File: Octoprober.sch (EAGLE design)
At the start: 140 parts, among them J1 10118193-0001LF, J2 26-60-4020, P1 TC33X-2-103E, SW1 101-0134-EV, SW2 EVQ-Q2203W, SW3 EVQ-Q2203W, SW4 EVQ-Q2203W, SW5 EVQ-Q2203W, U1 P8X32A-M44, U10 MAX31855KASA+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

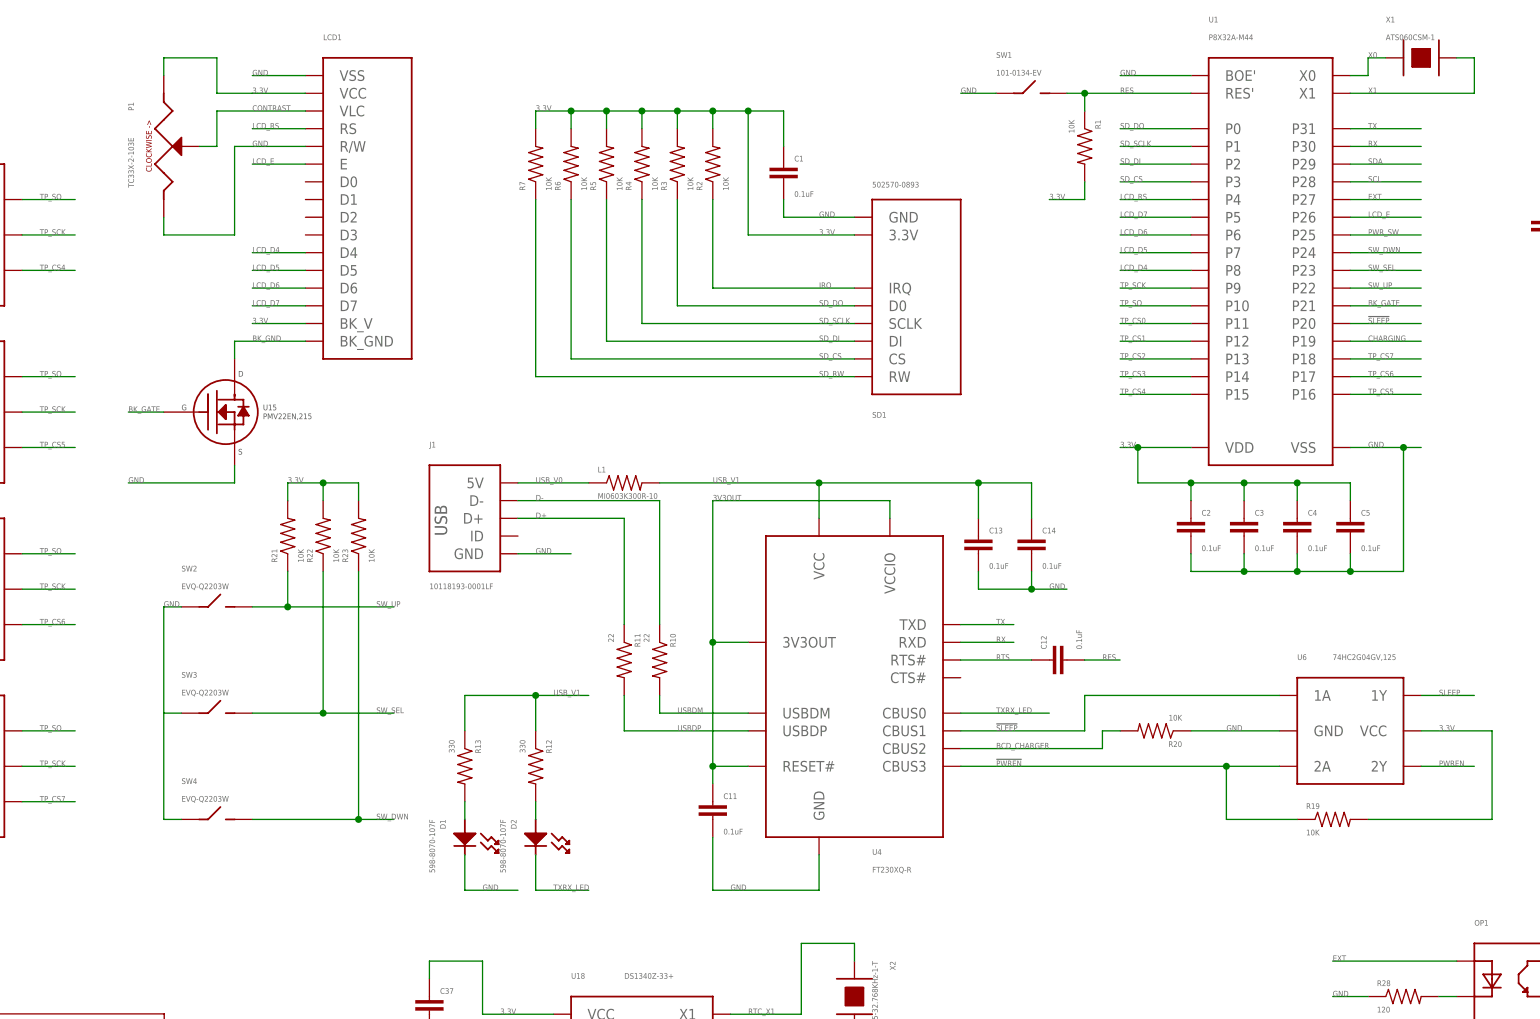
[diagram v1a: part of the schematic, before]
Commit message: Changed FT230X RST to be controlled by PROP
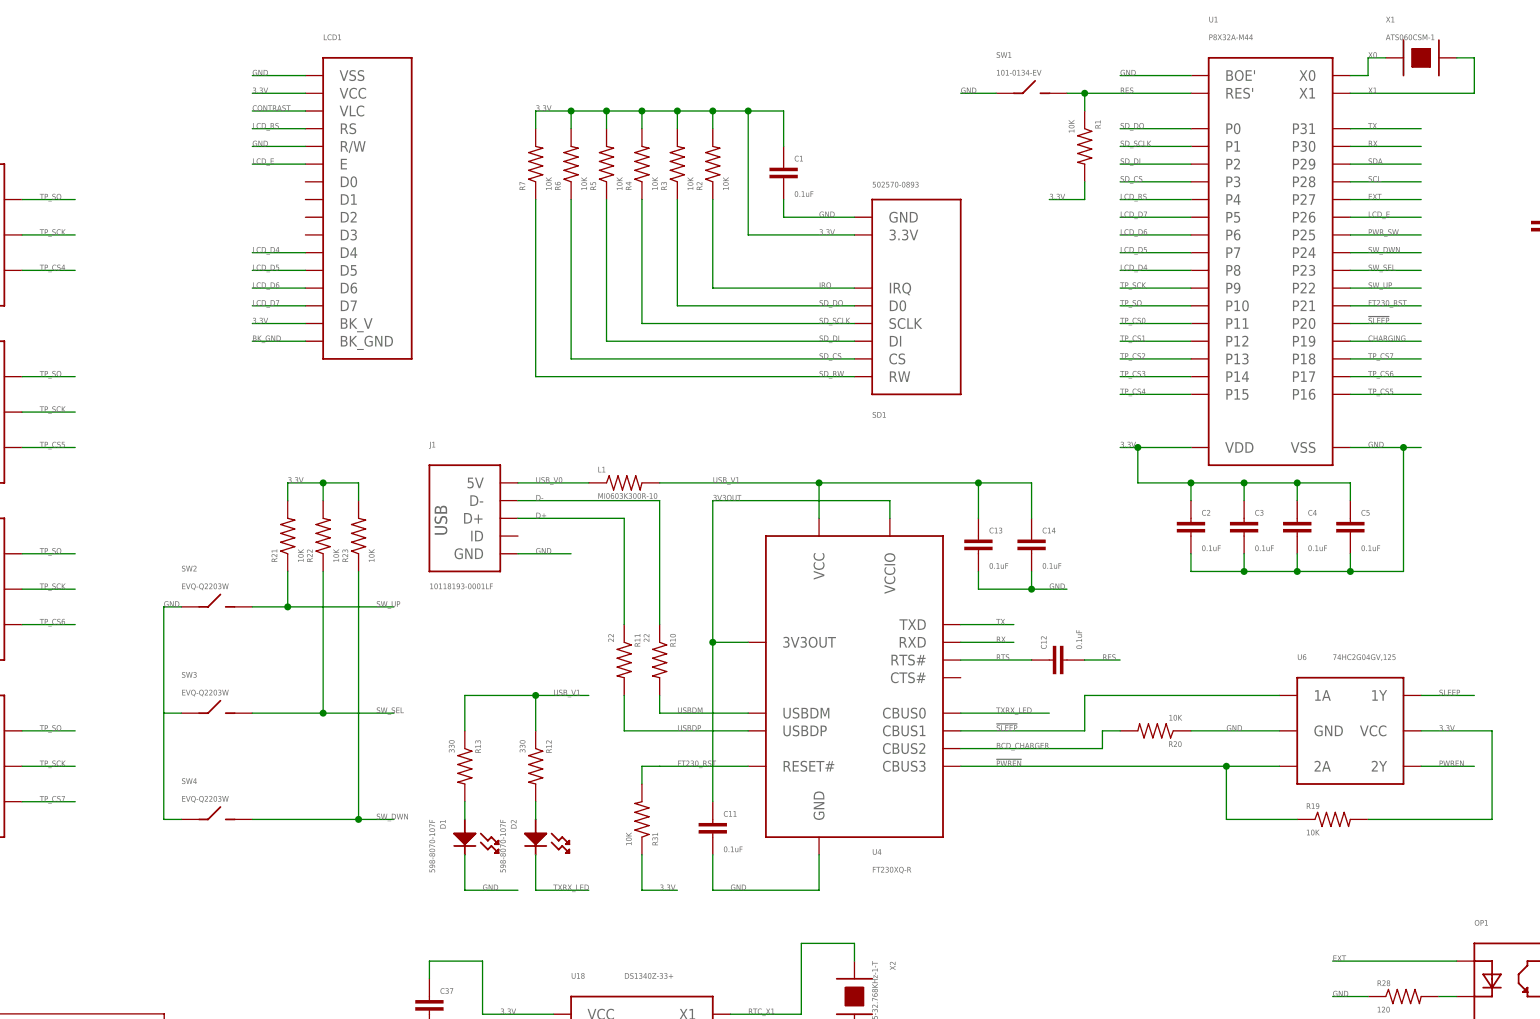
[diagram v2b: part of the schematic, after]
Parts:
- removed P1: TC33X-2-103E, PP_Passives:TC33X-1TC33X-1
- removed U15: PMV22EN,215, PP_DiscreteSemi:MOSFET_N-CHANNEL_SINGLESOT-23
- added R31: 10K, PP_Passives:RESISTOR0402
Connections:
- removed net BK_GATE: U1.P21, U15.GATE
- new net FT230_RST: R31.2, U1.P21, U4.RESET#
- net 3.3V: now also R31.1; no longer P1.1_CCW
- net 3V3OUT: no longer U4.RESET#
- net BK_GND: no longer U15.DRAIN
- net CONTRAST: no longer P1.2_WIPER
- net GND: no longer P1.3_CW, U15.SOURCE
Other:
- moved on the sheet: C11
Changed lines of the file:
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@@
 </part>
 <part name="LCD1" library="PP_Displays" deviceset="HD44780_LCD" device="1602_COUNTERSINK"/>
-<part name="P1" library="PP_Passives" deviceset="TC33X-1" device="TC33X-1" value="TC33X-2-103E"/>
 <part name="U7" library="PP_Sensors" deviceset="MAX31855" device="SO-8" value="MAX31855KASA+"/>
 <part name="C15" library="PP_Passives" deviceset="CAPACITOR_NON_POLAR" device="0402" value="0.1uF"/>
@@
 <part name="R19" library="PP_Passives" deviceset="RESISTOR" device="0402" value="10K"/>
 <part name="R20" library="PP_Passives" deviceset="RESISTOR" device="0402" value="10K"/>
-<part name="U15" library="PP_DiscreteSemi" deviceset="MOSFET_N-CHANNEL_SINGLE" device="SOT-23" value="PMV22EN,215"/>
 <part name="SW2" library="PP_Electromechanical" deviceset="SPST" device="EVQ-Q2203W" value="EVQ-Q2203W"/>
 <part name="SW3" library="PP_Electromechanical" deviceset="SPST" device="EVQ-Q2203W" value="EVQ-Q2203W"/>
@@
 <part name="C39" library="PP_Passives" deviceset="CAPACITOR_NON_POLAR" device="0402" value="0.1uF"/>
 <part name="U19" library="PP_DigitalIC" deviceset="MCP3021" device="SOT-23A" value="MCP3021A5T-E/OT"/>
+<part name="R31" library="PP_Passives" deviceset="RESISTOR" device="0402" value="10K"/>
 </parts>
 <sheets>
@@
 <instance part="L1" gate="G$1" x="-93.98" y="-27.94"/>
 <instance part="U4" gate="G$1" x="-60.96" y="-58.42"/>
-<instance part="C11" gate="G$1" x="-81.28" y="-73.66"/>
+<instance part="C11" gate="G$1" x="-81.28" y="-76.2"/>
 <instance part="R10" gate="G$1" x="-88.9" y="-53.34" rot="R270"/>
 <instance part="R11" gate="G$1" x="-93.98" y="-53.34" rot="R270"/>
@@
 </instance>
 <instance part="LCD1" gate="G$1" x="-129.54" y="12.7"/>
-<instance part="P1" gate="G$1" x="-160.02" y="20.32" rot="R270"/>
 <instance part="U7" gate="G$1" x="-292.1" y="7.62"/>
 <instance part="C15" gate="G$1" x="-325.12" y="10.16"/>
@@
 <instance part="R19" gate="G$1" x="7.62" y="-76.2"/>
 <instance part="R20" gate="G$1" x="-17.78" y="-63.5" rot="R180"/>
-<instance part="U15" gate="G$1" x="-149.86" y="-17.78"/>
 <instance part="SW2" gate="G$1" x="-152.4" y="-45.72"/>
 <instance part="SW3" gate="G$1" x="-152.4" y="-60.96"/>
@@
 <instance part="C39" gate="G$1" x="86.36" y="-116.84"/>
 <instance part="U19" gate="G$1" x="119.38" y="-109.22"/>
+<instance part="R31" gate="G$1" x="-91.44" y="-76.2" rot="MR90"/>
 </instances>
 <busses>
@@
 </segment>
 <segment>
-<wire x1="-81.28" y1="-78.74" x2="-81.28" y2="-86.36" width="0.1524" layer="91"/>
+<wire x1="-81.28" y1="-81.28" x2="-81.28" y2="-86.36" width="0.1524" layer="91"/>
 <pinref part="U4" gate="G$1" pin="GND"/>
 <wire x1="-81.28" y1="-86.36" x2="-66.04" y2="-86.36" width="0.1524" layer="91"/>
@@
 <segment>
 <pinref part="LCD1" gate="G$1" pin="R/W"/>
-<wire x1="-149.86" y1="20.32" x2="-139.7" y2="20.32" width="0.1524" layer="91"/>
+<wire x1="-147.32" y1="20.32" x2="-139.7" y2="20.32" width="0.1524" layer="91"/>
 <label x="-147.32" y="20.32" size="0.8128" layer="95" font="vector"/>
-<pinref part="P1" gate="G$1" pin="3_CW"/>
-<wire x1="-160.02" y1="10.16" x2="-160.02" y2="7.62" width="0.1524" layer="91"/>
-<wire x1="-160.02" y1="7.62" x2="-149.86" y2="7.62" width="0.1524" layer="91"/>
-<wire x1="-149.86" y1="7.62" x2="-149.86" y2="20.32" width="0.1524" layer="91"/>
 </segment>
 <segment>
@@
 <label x="-7.62" y="-63.5" size="0.8128" layer="95" font="vector"/>
 <pinref part="R20" gate="G$1" pin="1"/>
-</segment>
-<segment>
-<pinref part="U15" gate="G$1" pin="SOURCE"/>
-<wire x1="-149.86" y1="-25.4" x2="-149.86" y2="-27.94" width="0.1524" layer="91"/>
-<wire x1="-149.86" y1="-27.94" x2="-165.1" y2="-27.94" width="0.1524" layer="91"/>
-<label x="-165.1" y="-27.94" size="0.8128" layer="95" font="vector"/>
 </segment>
 <segment>
@@
 <wire x1="-139.7" y1="27.94" x2="-147.32" y2="27.94" width="0.1524" layer="91"/>
 <label x="-147.32" y="27.94" size="0.8128" layer="95" font="vector"/>
-<pinref part="P1" gate="G$1" pin="1_CCW"/>
-<wire x1="-160.02" y1="30.48" x2="-160.02" y2="33.02" width="0.1524" layer="91"/>
-<wire x1="-160.02" y1="33.02" x2="-152.4" y2="33.02" width="0.1524" layer="91"/>
-<wire x1="-152.4" y1="33.02" x2="-152.4" y2="27.94" width="0.1524" layer="91"/>
-<wire x1="-152.4" y1="27.94" x2="-147.32" y2="27.94" width="0.1524" layer="91"/>
+</segment>
+<segment>
+<pinref part="R31" gate="G$1" pin="1"/>
+<wire x1="-91.44" y1="-81.28" x2="-91.44" y2="-86.36" width="0.1524" layer="91"/>
+<wire x1="-91.44" y1="-86.36" x2="-86.36" y2="-86.36" width="0.1524" layer="91"/>
+<label x="-88.9" y="-86.36" size="0.8128" layer="95" font="vector"/>
 </segment>
 </net>
@@
 <wire x1="-81.28" y1="-30.48" x2="-81.28" y2="-50.8" width="0.1524" layer="91"/>
 <label x="-81.28" y="-30.48" size="0.8128" layer="95" font="vector"/>
-<pinref part="U4" gate="G$1" pin="RESET#"/>
-<wire x1="-81.28" y1="-50.8" x2="-81.28" y2="-68.58" width="0.1524" layer="91"/>
-<wire x1="-81.28" y1="-68.58" x2="-81.28" y2="-71.12" width="0.1524" layer="91"/>
-<wire x1="-76.2" y1="-68.58" x2="-81.28" y2="-68.58" width="0.1524" layer="91"/>
+<wire x1="-81.28" y1="-50.8" x2="-81.28" y2="-73.66" width="0.1524" layer="91"/>
 <pinref part="U4" gate="G$1" pin="3V3OUT"/>
 <wire x1="-76.2" y1="-50.8" x2="-81.28" y2="-50.8" width="0.1524" layer="91"/>
-<junction x="-81.28" y="-68.58"/>
 <junction x="-81.28" y="-50.8"/>
 </segment>
@@
 <segment>
 <pinref part="LCD1" gate="G$1" pin="VLC"/>
-<wire x1="-154.94" y1="20.32" x2="-152.4" y2="20.32" width="0.1524" layer="91"/>
-<wire x1="-152.4" y1="20.32" x2="-152.4" y2="25.4" width="0.1524" layer="91"/>
-<wire x1="-152.4" y1="25.4" x2="-139.7" y2="25.4" width="0.1524" layer="91"/>
+<wire x1="-147.32" y1="25.4" x2="-139.7" y2="25.4" width="0.1524" layer="91"/>
 <label x="-147.32" y="25.4" size="0.8128" layer="95" font="vector"/>
-<pinref part="P1" gate="G$1" pin="2_WIPER"/>
 </segment>
 </net>
@@
 <segment>
 <pinref part="LCD1" gate="G$1" pin="BK_GND"/>
-<wire x1="-139.7" y1="-7.62" x2="-149.86" y2="-7.62" width="0.1524" layer="91"/>
+<wire x1="-139.7" y1="-7.62" x2="-147.32" y2="-7.62" width="0.1524" layer="91"/>
 <label x="-147.32" y="-7.62" size="0.8128" layer="95" font="vector"/>
-<pinref part="U15" gate="G$1" pin="DRAIN"/>
-<wire x1="-149.86" y1="-10.16" x2="-149.86" y2="-7.62" width="0.1524" layer="91"/>
 </segment>
 </net>
@@
 </segment>
 </net>
-<net name="BK_GATE" class="0">
-<segment>
-<pinref part="U15" gate="G$1" pin="GATE"/>
-<wire x1="-160.02" y1="-17.78" x2="-165.1" y2="-17.78" width="0.1524" layer="91"/>
-<label x="-165.1" y="-17.78" size="0.8128" layer="95" font="vector"/>
-</segment>
+<net name="FT230_RST" class="0">
 <segment>
 <pinref part="U1" gate="G$1" pin="P21"/>
@@
 <label x="12.7" y="-2.54" size="0.8128" layer="95" font="vector"/>
 </segment>
-</net>
+<segment>
+<pinref part="U4" gate="G$1" pin="RESET#"/>
+<wire x1="-76.2" y1="-68.58" x2="-88.9" y2="-68.58" width="0.1524" layer="91"/>
+<wire x1="-88.9" y1="-68.58" x2="-91.44" y2="-68.58" width="0.1524" layer="91"/>
+<pinref part="R31" gate="G$1" pin="2"/>
+<wire x1="-91.44" y1="-68.58" x2="-91.44" y2="-71.12" width="0.1524" layer="91"/>
+<label x="-86.36" y="-68.58" size="0.8128" layer="95" font="vector"/>
+</segment>
+</net>

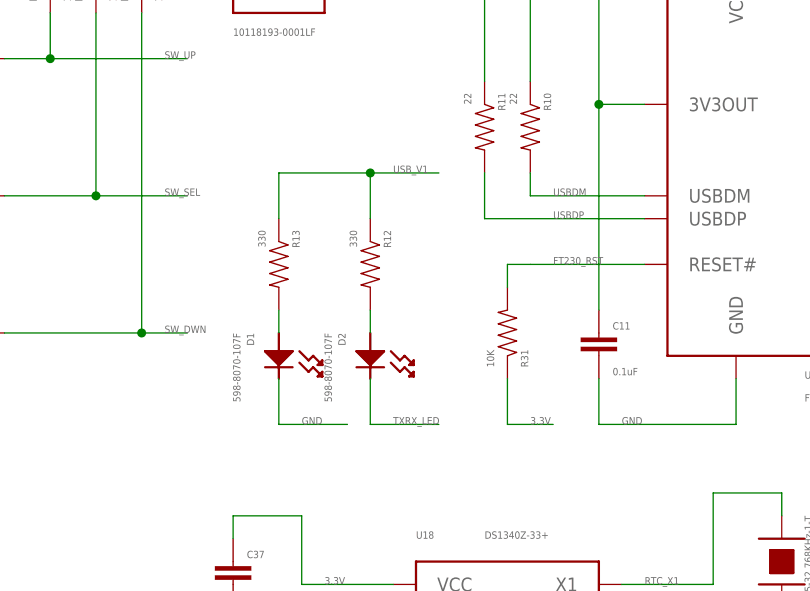
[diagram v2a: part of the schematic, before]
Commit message: Added cap to FT230X RST line.
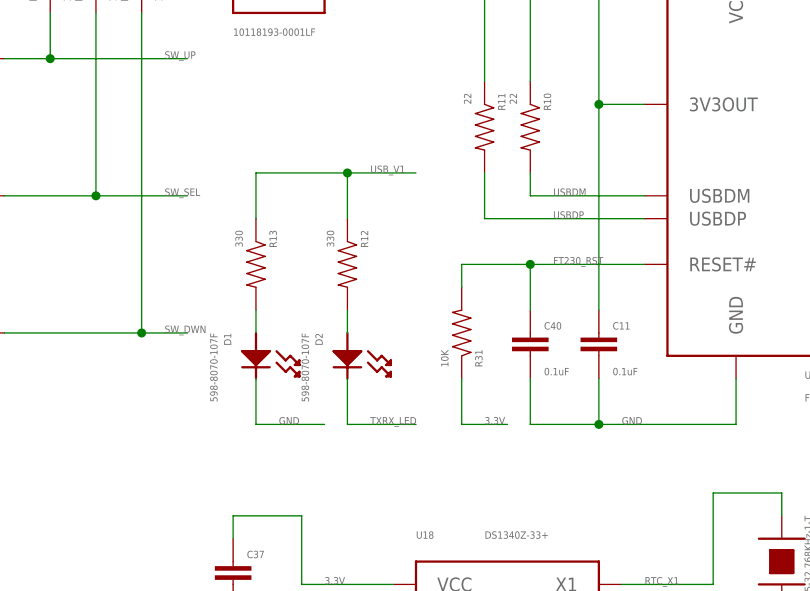
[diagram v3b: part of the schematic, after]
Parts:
- added C40: 0.1uF, PP_Passives:CAPACITOR_NON_POLAR0402
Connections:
- net FT230_RST: now also C40.1
- net GND: now also C40.2
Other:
- moved on the sheet: D1, D2, R12, R13, R31
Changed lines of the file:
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@@
 <part name="U19" library="PP_DigitalIC" deviceset="MCP3021" device="SOT-23A" value="MCP3021A5T-E/OT"/>
 <part name="R31" library="PP_Passives" deviceset="RESISTOR" device="0402" value="10K"/>
+<part name="C40" library="PP_Passives" deviceset="CAPACITOR_NON_POLAR" device="0402" value="0.1uF"/>
 </parts>
 <sheets>
@@
 <instance part="R11" gate="G$1" x="-93.98" y="-53.34" rot="R270"/>
 <instance part="C12" gate="G$1" x="-33.02" y="-53.34" rot="R90"/>
-<instance part="D1" gate="G$1" x="-116.84" y="-78.74" rot="R270"/>
-<instance part="D2" gate="G$1" x="-106.68" y="-78.74" rot="R270"/>
-<instance part="R12" gate="G$1" x="-106.68" y="-68.58" rot="R270"/>
-<instance part="R13" gate="G$1" x="-116.84" y="-68.58" rot="R270"/>
+<instance part="D1" gate="G$1" x="-119.38" y="-78.74" rot="R270"/>
+<instance part="D2" gate="G$1" x="-109.22" y="-78.74" rot="R270"/>
+<instance part="R12" gate="G$1" x="-109.22" y="-68.58" rot="R270"/>
+<instance part="R13" gate="G$1" x="-119.38" y="-68.58" rot="R270"/>
 <instance part="C13" gate="G$1" x="-43.18" y="-35.56"/>
 <instance part="C14" gate="G$1" x="-35.56" y="-35.56"/>
@@
 <instance part="C39" gate="G$1" x="86.36" y="-116.84"/>
 <instance part="U19" gate="G$1" x="119.38" y="-109.22"/>
-<instance part="R31" gate="G$1" x="-91.44" y="-76.2" rot="MR90"/>
+<instance part="R31" gate="G$1" x="-96.52" y="-76.2" rot="MR90"/>
+<instance part="C40" gate="G$1" x="-88.9" y="-76.2"/>
 </instances>
 <busses>
@@
 <segment>
 <pinref part="D1" gate="G$1" pin="CATHODE"/>
-<wire x1="-116.84" y1="-81.28" x2="-116.84" y2="-86.36" width="0.1524" layer="91"/>
-<wire x1="-116.84" y1="-86.36" x2="-109.22" y2="-86.36" width="0.1524" layer="91"/>
-<label x="-114.3" y="-86.36" size="0.8128" layer="95" font="vector"/>
+<wire x1="-119.38" y1="-81.28" x2="-119.38" y2="-86.36" width="0.1524" layer="91"/>
+<wire x1="-119.38" y1="-86.36" x2="-111.76" y2="-86.36" width="0.1524" layer="91"/>
+<label x="-116.84" y="-86.36" size="0.8128" layer="95" font="vector"/>
 </segment>
 <segment>
@@
 <pinref part="C11" gate="G$1" pin="2"/>
 <label x="-78.74" y="-86.36" size="0.8128" layer="95" font="vector"/>
+<pinref part="C40" gate="G$1" pin="2"/>
+<wire x1="-88.9" y1="-81.28" x2="-88.9" y2="-86.36" width="0.1524" layer="91"/>
+<wire x1="-88.9" y1="-86.36" x2="-81.28" y2="-86.36" width="0.1524" layer="91"/>
+<junction x="-81.28" y="-86.36"/>
 </segment>
 <segment>
@@
 <segment>
 <pinref part="R31" gate="G$1" pin="1"/>
-<wire x1="-91.44" y1="-81.28" x2="-91.44" y2="-86.36" width="0.1524" layer="91"/>
-<wire x1="-91.44" y1="-86.36" x2="-86.36" y2="-86.36" width="0.1524" layer="91"/>
-<label x="-88.9" y="-86.36" size="0.8128" layer="95" font="vector"/>
+<wire x1="-96.52" y1="-81.28" x2="-96.52" y2="-86.36" width="0.1524" layer="91"/>
+<wire x1="-96.52" y1="-86.36" x2="-91.44" y2="-86.36" width="0.1524" layer="91"/>
+<label x="-93.98" y="-86.36" size="0.8128" layer="95" font="vector"/>
 </segment>
 </net>
@@
 <segment>
 <pinref part="D2" gate="G$1" pin="CATHODE"/>
-<wire x1="-106.68" y1="-81.28" x2="-106.68" y2="-86.36" width="0.1524" layer="91"/>
-<wire x1="-106.68" y1="-86.36" x2="-99.06" y2="-86.36" width="0.1524" layer="91"/>
-<label x="-104.14" y="-86.36" size="0.8128" layer="95" font="vector"/>
+<wire x1="-109.22" y1="-81.28" x2="-109.22" y2="-86.36" width="0.1524" layer="91"/>
+<wire x1="-109.22" y1="-86.36" x2="-101.6" y2="-86.36" width="0.1524" layer="91"/>
+<label x="-106.68" y="-86.36" size="0.8128" layer="95" font="vector"/>
 </segment>
 <segment>
@@
 <pinref part="D2" gate="G$1" pin="ANODE"/>
 <pinref part="R12" gate="G$1" pin="2"/>
-<wire x1="-106.68" y1="-76.2" x2="-106.68" y2="-73.66" width="0.1524" layer="91"/>
+<wire x1="-109.22" y1="-76.2" x2="-109.22" y2="-73.66" width="0.1524" layer="91"/>
 </segment>
 </net>
@@
 <pinref part="D1" gate="G$1" pin="ANODE"/>
 <pinref part="R13" gate="G$1" pin="2"/>
-<wire x1="-116.84" y1="-76.2" x2="-116.84" y2="-73.66" width="0.1524" layer="91"/>
+<wire x1="-119.38" y1="-76.2" x2="-119.38" y2="-73.66" width="0.1524" layer="91"/>
 </segment>
 </net>
@@
 <segment>
 <pinref part="R13" gate="G$1" pin="1"/>
-<wire x1="-116.84" y1="-63.5" x2="-116.84" y2="-58.42" width="0.1524" layer="91"/>
-<wire x1="-116.84" y1="-58.42" x2="-106.68" y2="-58.42" width="0.1524" layer="91"/>
+<wire x1="-119.38" y1="-63.5" x2="-119.38" y2="-58.42" width="0.1524" layer="91"/>
+<wire x1="-119.38" y1="-58.42" x2="-109.22" y2="-58.42" width="0.1524" layer="91"/>
 <pinref part="R12" gate="G$1" pin="1"/>
-<wire x1="-106.68" y1="-63.5" x2="-106.68" y2="-58.42" width="0.1524" layer="91"/>
-<wire x1="-106.68" y1="-58.42" x2="-99.06" y2="-58.42" width="0.1524" layer="91"/>
-<label x="-104.14" y="-58.42" size="0.8128" layer="95" font="vector"/>
-<junction x="-106.68" y="-58.42"/>
+<wire x1="-109.22" y1="-63.5" x2="-109.22" y2="-58.42" width="0.1524" layer="91"/>
+<wire x1="-109.22" y1="-58.42" x2="-101.6" y2="-58.42" width="0.1524" layer="91"/>
+<label x="-106.68" y="-58.42" size="0.8128" layer="95" font="vector"/>
+<junction x="-109.22" y="-58.42"/>
 </segment>
 <segment>
@@
 <pinref part="U4" gate="G$1" pin="RESET#"/>
 <wire x1="-76.2" y1="-68.58" x2="-88.9" y2="-68.58" width="0.1524" layer="91"/>
-<wire x1="-88.9" y1="-68.58" x2="-91.44" y2="-68.58" width="0.1524" layer="91"/>
 <pinref part="R31" gate="G$1" pin="2"/>
-<wire x1="-91.44" y1="-68.58" x2="-91.44" y2="-71.12" width="0.1524" layer="91"/>
+<wire x1="-88.9" y1="-68.58" x2="-96.52" y2="-68.58" width="0.1524" layer="91"/>
+<wire x1="-96.52" y1="-68.58" x2="-96.52" y2="-71.12" width="0.1524" layer="91"/>
 <label x="-86.36" y="-68.58" size="0.8128" layer="95" font="vector"/>
-</segment>
-</net>
+<pinref part="C40" gate="G$1" pin="1"/>
+<wire x1="-88.9" y1="-73.66" x2="-88.9" y2="-68.58" width="0.1524" layer="91"/>
+<junction x="-88.9" y="-68.58"/>
+</segment>
+</net>
